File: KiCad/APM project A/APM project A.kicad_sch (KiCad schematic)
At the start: 20 parts, among them M1 DC_MOTOR, M2 DC_MOTOR, U1 ultrasone_sensor, U2 ultrasone_sensor

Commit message: opleverset deels gemaakt
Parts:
- removed bit_shifter: 74HC165, symbol 74xx:74HC165
- motor_driver: value L298N -> L293D
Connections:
- net D3 is gone; now on net ESP2_IO13: start_knop.2
- net D4 is gone; now on net ESP2_IO4: route_knop.2
- net D5 is gone; now on net ESP2_IO2: pakketdetectie.2 (Pin_2)
- net OUT_achter is gone; now on net ESP2_IO35: IR_achter.3 (Pin_3)
- net OUT_links is gone; now on net ESP2_IO34: IR_links.3 (Pin_3)
- net OUT_rechts is gone; now on net ESP2_IO33: IR_rechts.3 (Pin_3)
- net GND: now also motor_driver.1 (SENSE_A), motor_driver.15 (SENSE_B)
- net MOT_A+: now also motor_driver.13 (OUT3), motor_driver.2 (OUT1)
- net MOT_A-: now also motor_driver.14 (OUT4), motor_driver.3 (OUT2)
- net ESP2_IO13: now reaches ESP_2.16 (IO13)
- net ESP2_IO2: now reaches ESP_2.24 (IO2)
- net ESP2_IO4: now reaches ESP_2.26 (IO4)
- net ESP2_IO34: now reaches ESP_2.6 (IO34)
- net ESP2_IO35: now reaches ESP_2.7 (IO35)
- net ESP2_IO33: now reaches ESP_2.9 (IO33)
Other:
- moved on the sheet: D1, ESP_1, ESP_2, IR_achter, IR_links, IR_rechts, MFRC522, R1, R2, R3, motor_driver, nood_knop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

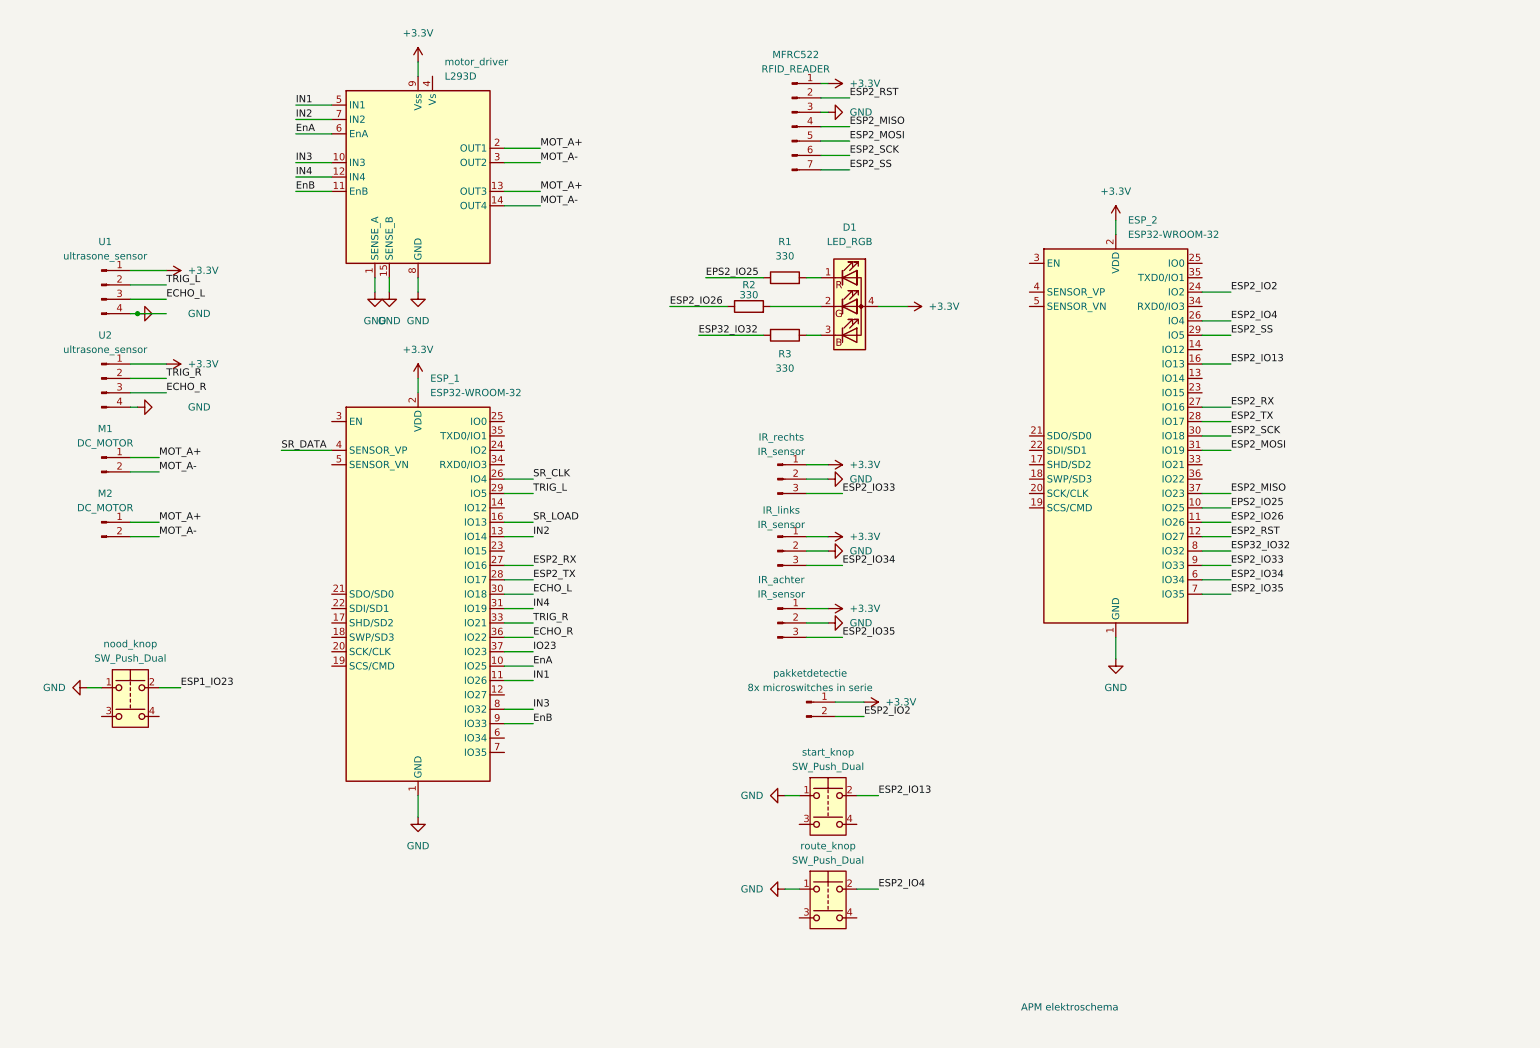
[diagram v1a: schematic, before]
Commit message: elektrisch schema aangepast
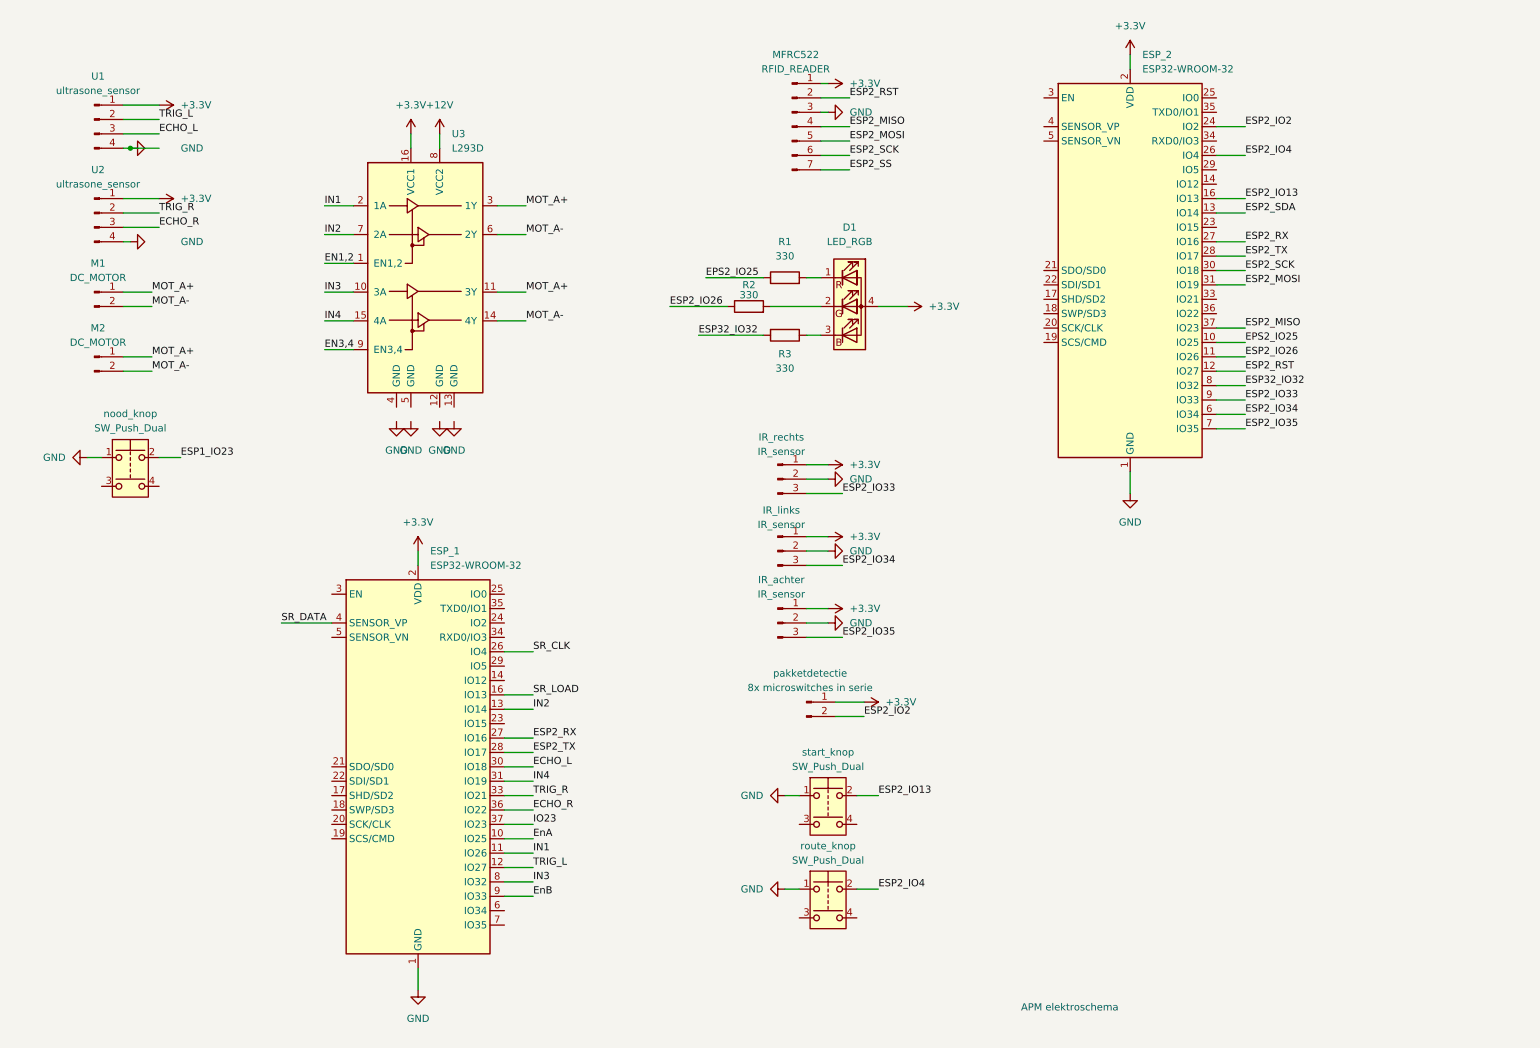
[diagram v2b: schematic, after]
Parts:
- removed motor_driver: L293D, Package_TO_SOT_THT:TO-220-15_P2.54x5.08mm_StaggerOdd_Lead4.58mm_Vertical, symbol Driver_Motor:L298N
- added U3: L293D, Package_DIP:DIP-16_W7.62mm, symbol Driver_Motor:L293D
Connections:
- net +3.3V: now also U3.16 (VCC1)
- net ESP2_SS: no longer ESP_2.29 (IO5)
- net IN1: now also U3.2 (1A)
- net IN2: now also U3.7 (2A)
- net IN3: now also U3.10 (3A)
- net IN4: now also U3.15 (4A)
- net MOT_A+: now also U3.11 (3Y), U3.3 (1Y)
- net MOT_A-: now also U3.14 (4Y), U3.6 (2Y)
- net TRIG_L: now also ESP_1.12 (IO27); no longer ESP_1.29 (IO5)
- net ESP2_SDA: now reaches ESP_2.13 (IO14)
- new net +12V: U3.8 (VCC2)
- new net EN1,2: U3.1 (EN1,2)
- new net EN3,4: U3.9 (EN3,4)
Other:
- moved on the sheet: ESP_1, ESP_2, M1, M2, U1, U2, nood_knop

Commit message: .
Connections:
- net GND: now also U3.12 (GND), U3.13 (GND), U3.4 (GND), U3.5 (GND)
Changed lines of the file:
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@@
+	(wire
+		(pts
+			(xy 85.09 83.82) (xy 85.09 86.36)
+		)
+		(stroke
+			(width 0)
+			(type default)
+		)
+	)
 	(wire
 		(pts
@@
 	(wire
 		(pts
+			(xy 77.47 83.82) (xy 77.47 86.36)
+		)
+		(stroke
+			(width 0)
+			(type default)
+		)
+	)
+	(wire
+		(pts
 			(xy 132.08 60.96) (xy 142.24 60.96)
 		)
@@
 	(wire
 		(pts
+			(xy 87.63 83.82) (xy 87.63 86.36)
+		)
+		(stroke
+			(width 0)
+			(type default)
+		)
+	)
+	(wire
+		(pts
 			(xy 81.28 109.22) (xy 81.28 111.76)
 		)
@@
 		)
 		(stroke
+			(width 0)
+			(type default)
+		)
+	)
+	(wire
+		(pts
+			(xy 80.01 83.82) (xy 80.01 86.36)
+		)
+		(stroke

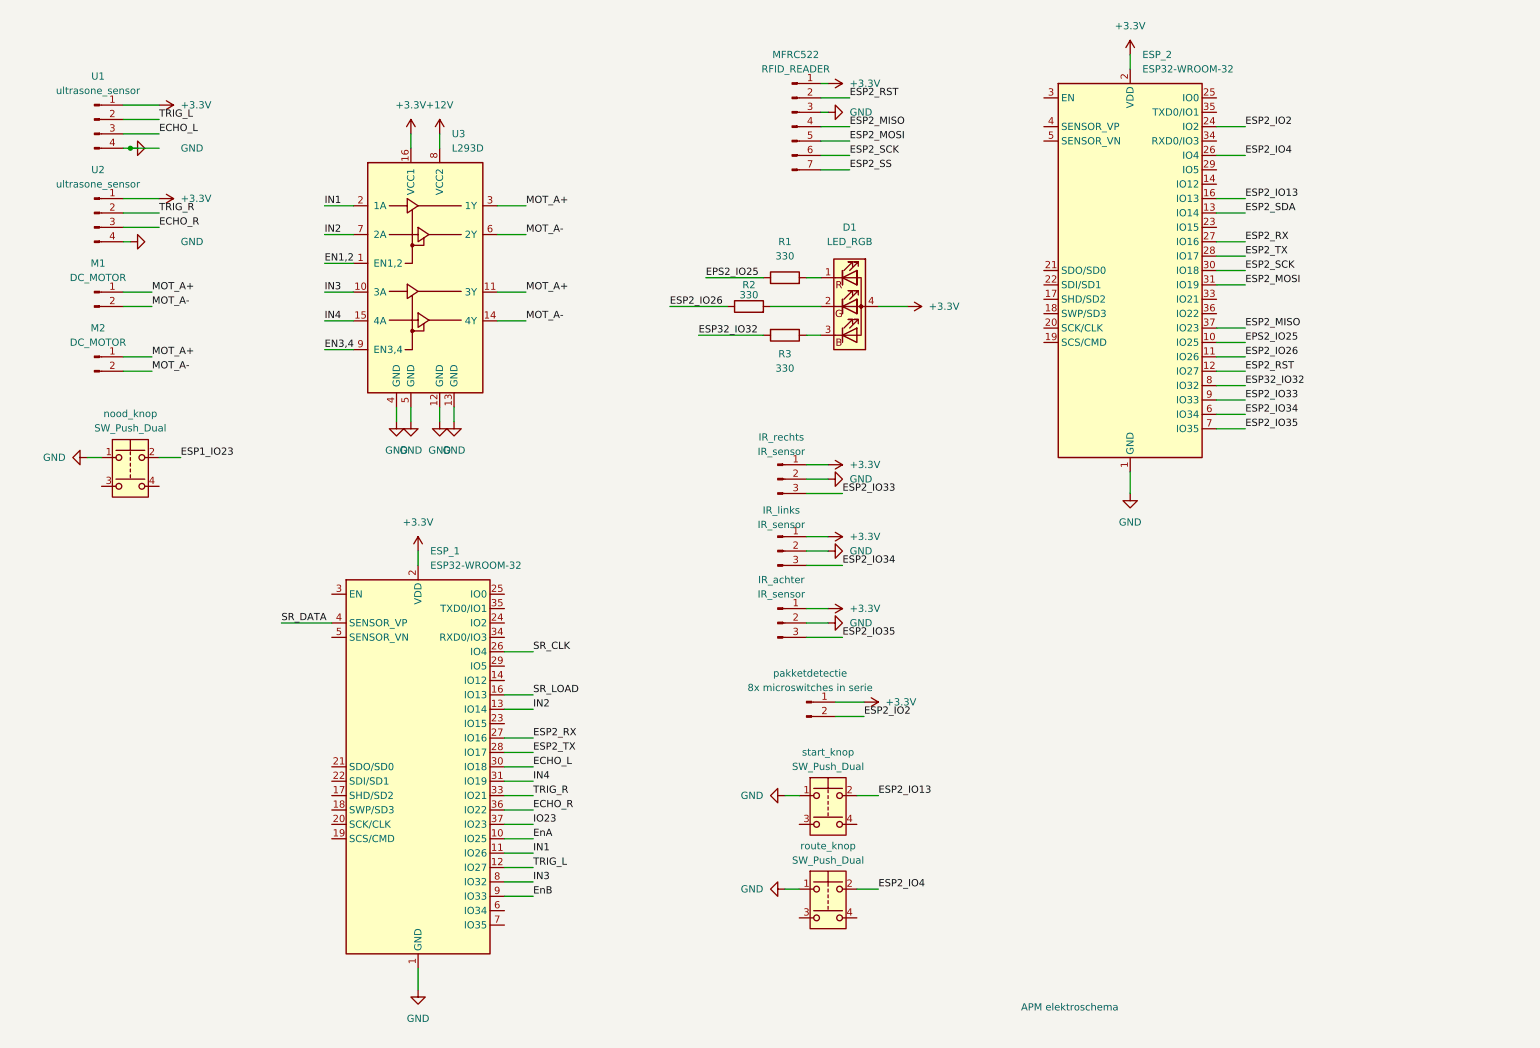
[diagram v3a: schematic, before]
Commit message: switch naar arduino mega, arduino ide code versie, elektrisch schema verwijderd
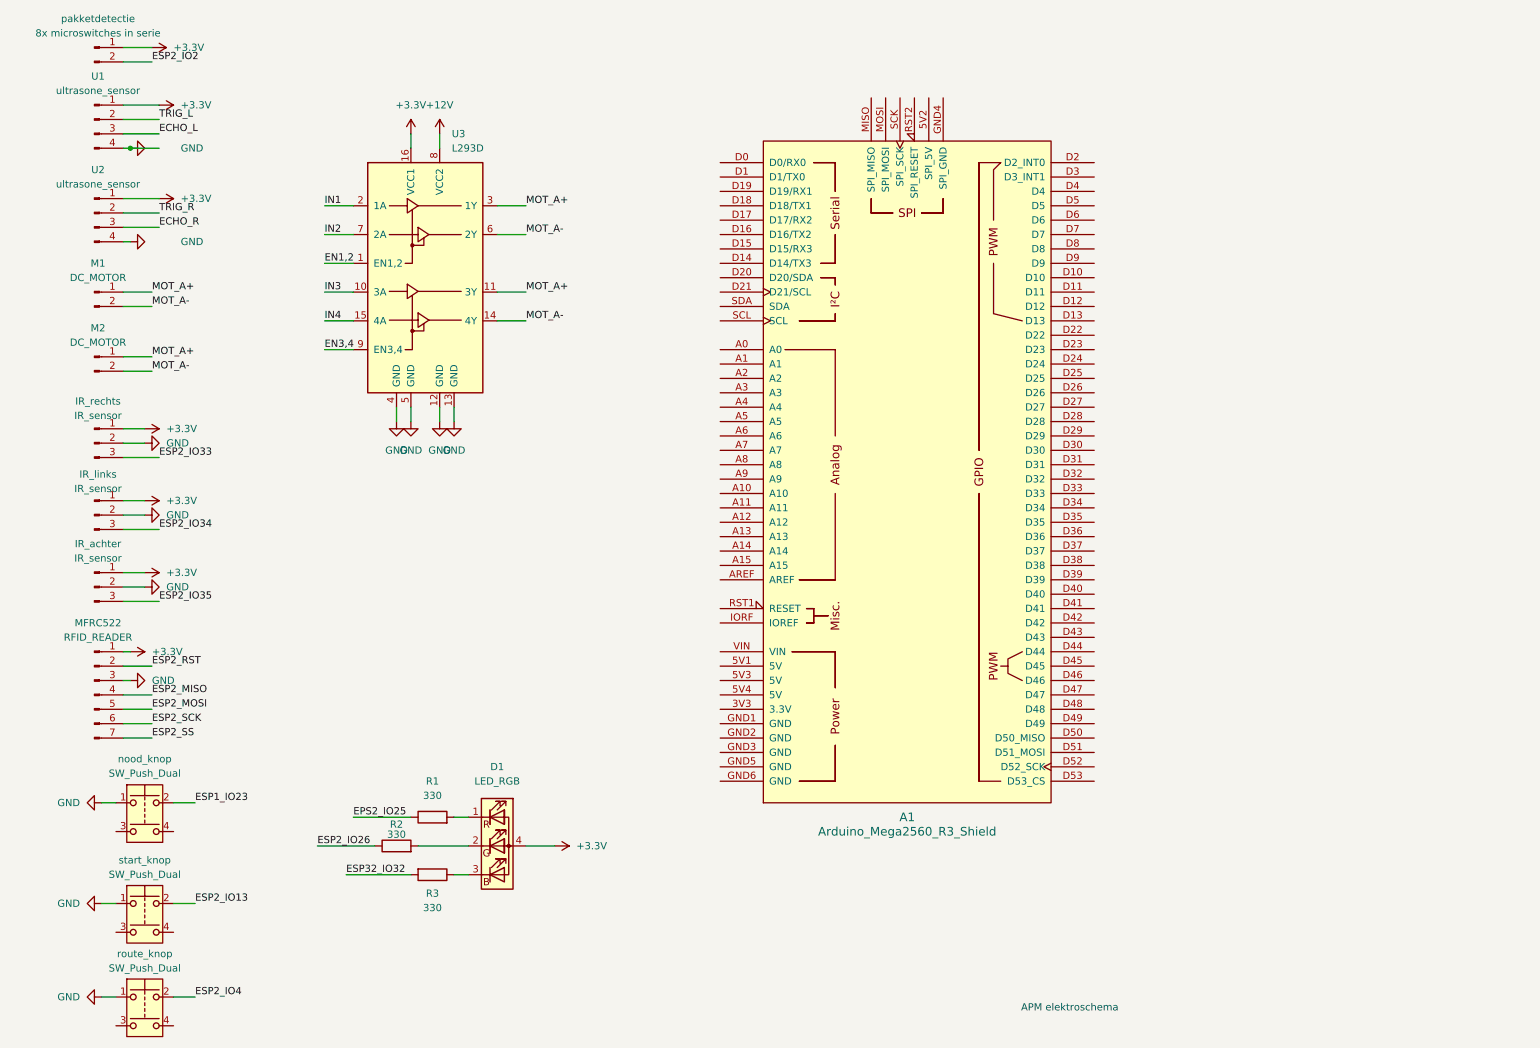
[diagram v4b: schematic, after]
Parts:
- removed ESP_1, ESP_2: ESP32-WROOM-32, RF_Module:ESP32-WROOM-32, symbol RF_Module:ESP32-WROOM-32
- added A1: Arduino_Mega2560_R3_Shield, PCM_arduino-library:Arduino_Mega2560_R3_Shield, symbol PCM_arduino-library:Arduino_Mega2560_R3_Shield
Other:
- moved on the sheet: D1, IR_achter, IR_links, IR_rechts, MFRC522, R1, R2, R3, nood_knop, pakketdetectie, route_knop, start_knop

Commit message: ontwerpdocument aangepast
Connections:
- net EPS2_IO25 is gone; now on net D25_ROOD: R1.1
- net ESP1_IO23 is gone; now on net D31: nood_knop.2
- net ESP2_IO13 is gone; now on net D32: start_knop.2
- net ESP2_IO2 is gone; now on net D34: pakketdetectie.2 (Pin_2)
- net ESP2_IO26 is gone; now on net D26_GROEN: R2.1
- net ESP2_IO33 is gone; now on net D23: IR_rechts.3 (Pin_3)
- net ESP2_IO34 is gone; now on net D22: IR_links.3 (Pin_3)
- net ESP2_IO35 is gone; now on net D24: IR_achter.3 (Pin_3)
- net ESP2_IO4 is gone; now on net D33: route_knop.2
- net ESP2_MISO is gone; now on net D50_MISO: MFRC522.4 (Pin_4)
- net ESP2_MOSI is gone; now on net D51_MOSI: MFRC522.5 (Pin_5)
- net ESP2_SCK is gone; now on net D52_SCK: MFRC522.6 (Pin_6)
- net ESP32_IO32 is gone; now on net D27_BLAUW: R3.2
- net ECHO_L: now also A1.D10
- net ECHO_R: now also A1.D8
- net EN1,2: now also A1.D11
- net EN3,4: now also A1.D12
- net IN1: now also A1.D5
- net IN2: now also A1.D6
- net IN3: now also A1.D4
- net IN4: now also A1.D3 (D3_INT1)
- net TRIG_L: now also A1.D9
- net TRIG_R: now also A1.D7
- net D22: now reaches A1.D22
- net D23: now reaches A1.D23
- net D24: now reaches A1.D24
- net D25_ROOD: now reaches A1.D25
- net D26_GROEN: now reaches A1.D26
- net D27_BLAUW: now reaches A1.D27
- net D31: now reaches A1.D31
- net D32: now reaches A1.D32
- net D33: now reaches A1.D33
- net D34: now reaches A1.D34
- net D49: now reaches A1.D49
- net D50_MISO: now reaches A1.D50 (D50_MISO)
- net D51_MOSI: now reaches A1.D51 (D51_MOSI)
- net D52_SCK: now reaches A1.D52 (D52_SCK)
- net ESP2_RST renamed D49_RST
- net ESP2_SS renamed D53_CS
